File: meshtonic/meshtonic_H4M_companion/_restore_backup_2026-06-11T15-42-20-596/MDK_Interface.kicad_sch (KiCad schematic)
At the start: 14 parts, among them J1 GROVE-CONNECTOR-DIP_4P-2.0_, J2 GROVE-CONNECTOR-DIP_4P-2.0_, J24 GROVE-CONNECTOR-SMD_4+2P-2.0_, J25 GROVE-CONNECTOR-DIP-90D_4P-2.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, J26 GROVE-CONNECTOR-DIP_4P-2.0_, J27 GROVE-CONNECTOR-DIP_4P-2.0_, J28 seeed:GROVE-HW4-2.0, J3 Conn_01x02, J4 Conn_01x02, J5 GROVE-CONNECTOR-DIP_4P-2.0_, J6 Conn_01x02

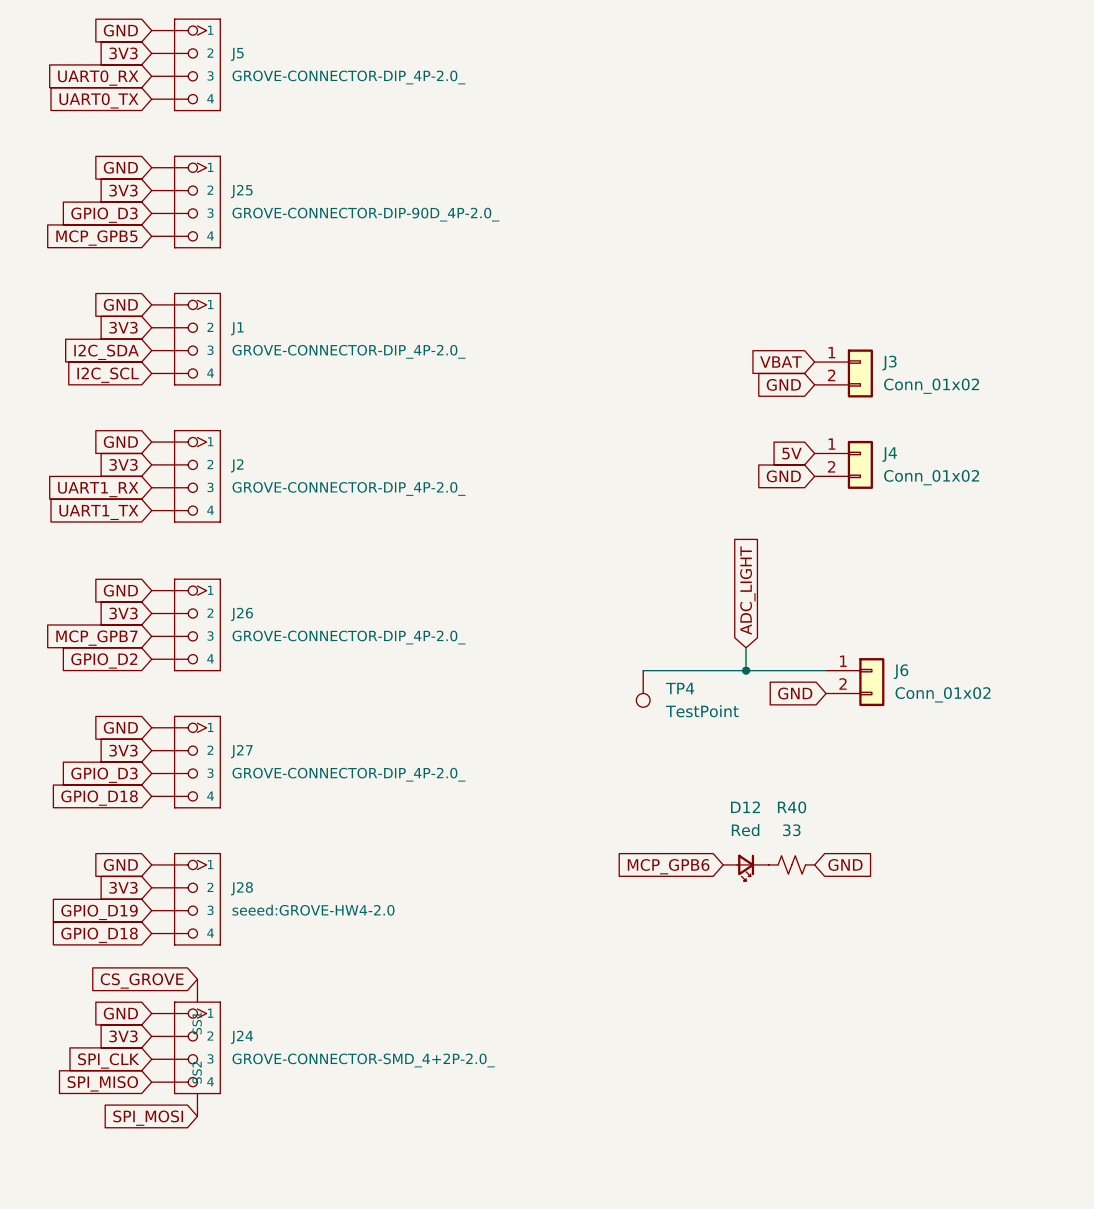
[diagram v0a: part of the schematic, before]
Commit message: adds meshtonic board
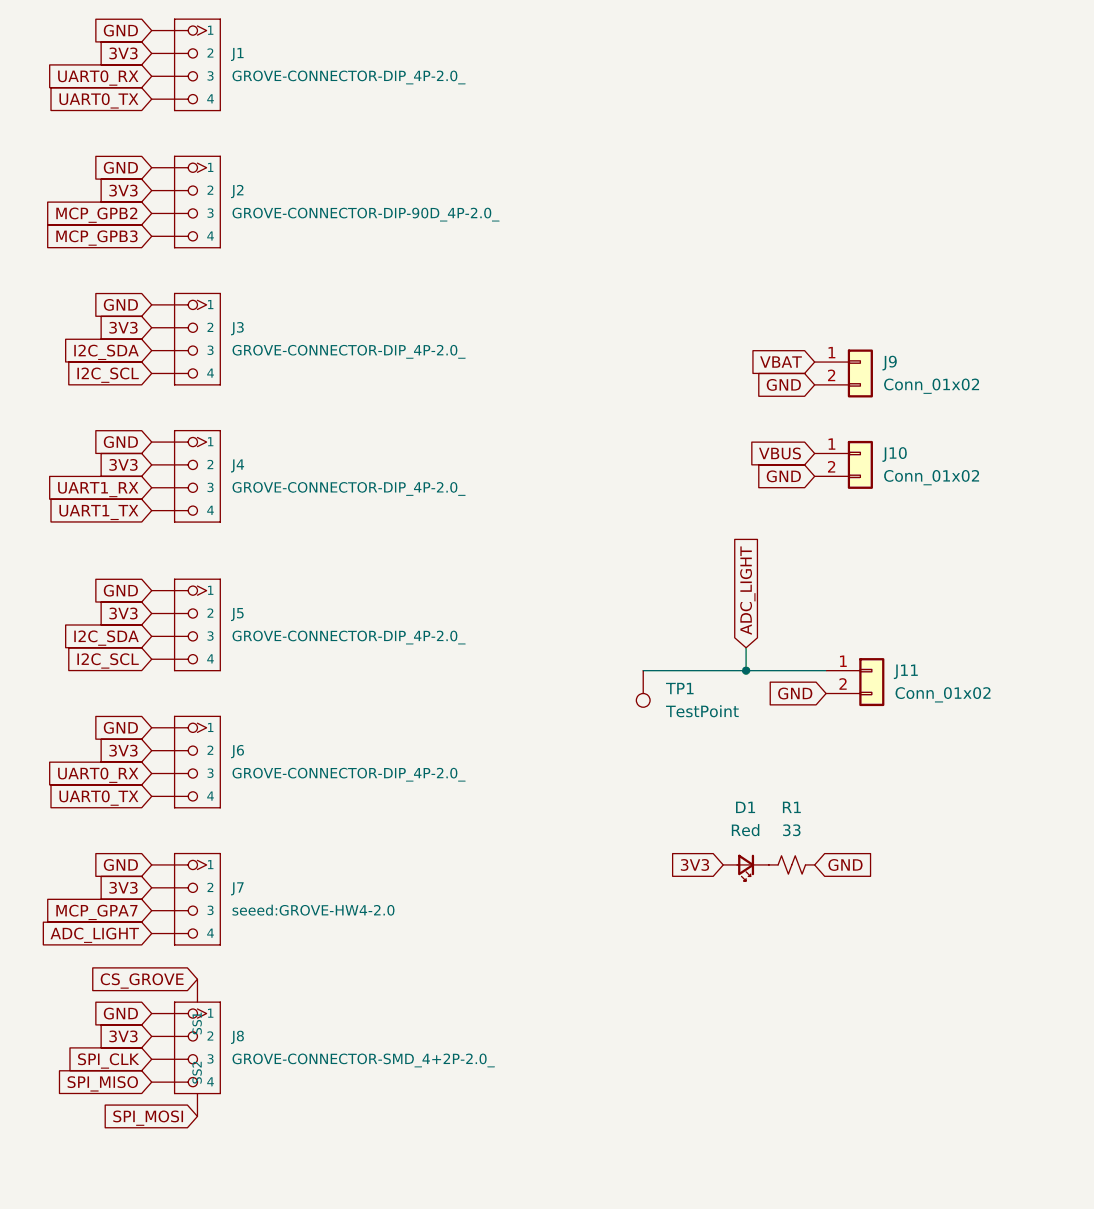
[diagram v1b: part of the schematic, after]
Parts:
- TP1: renamed from TP4; footprint (none) -> PCM_SparkFun-Connector:TestPoint-0.5mm
- renumbered D12 to D1, J5 to J1, J4 to J10, J6 to J11, J25 to J2, J1 to J3, J2 to J4, J26 to J5, J27 to J6, J28 to J7, J24 to J8, J3 to J9, R40 to R1
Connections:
- net GPIO_D2 is gone; now on net I2C_SCL: J5.4
- net MCP_GPB6 is gone; now on net 3V3: D1.2 (A)
- net MCP_GPB7 is gone; now on net I2C_SDA: J5.3
- net ADC_LIGHT: now also J7.4
- net UART0_RX: now also J6.3
- net UART0_TX: now also J6.4
- net 5V renamed VBUS
- removed net GPIO_D18: J6.4, J7.4
- net GPIO_D19 renamed MCP_GPA7
- net GPIO_D3 renamed MCP_GPB2
- net MCP_GPB2: no longer J6.3
- net MCP_GPB5 renamed MCP_GPB3
